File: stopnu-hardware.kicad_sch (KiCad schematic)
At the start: 19 parts, among them CN1 SM04B-SRSS-TB (LF)(SN), CN2 OQ0232510000G, CN3 OQ0232510000G, CN4 OQ0232510000G, CN5 OQ0232510000G, CN6 OQ0232510000G, CN7 OQ0232510000G, CN8 OQ0232510000G, J1 Conn_02x15_Odd_Even

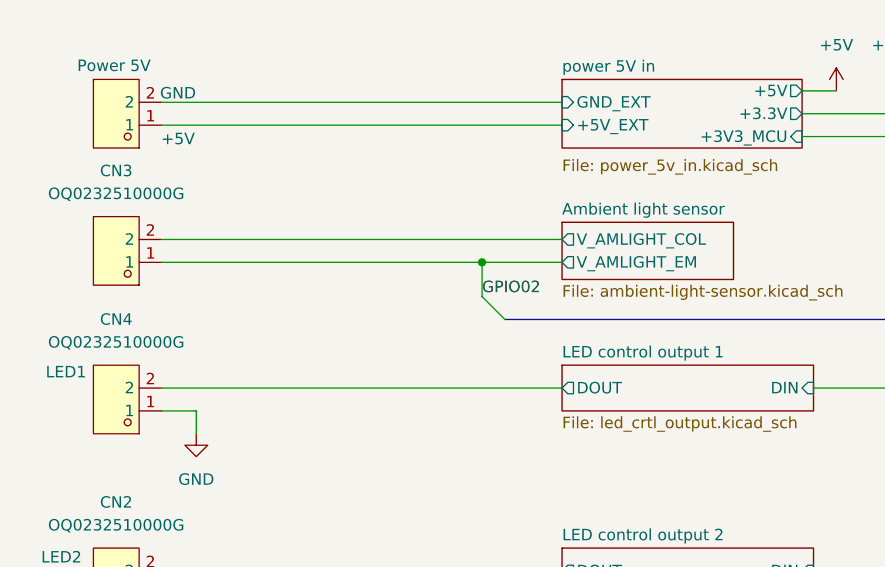
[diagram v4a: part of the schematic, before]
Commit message: Changed ambient light sensor to pull-up design.
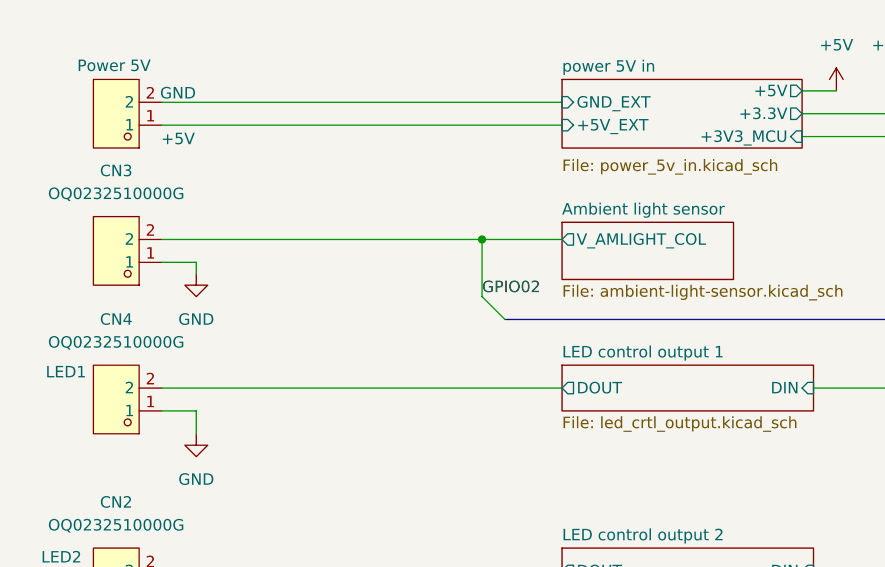
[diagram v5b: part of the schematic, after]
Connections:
- net Ambient light sensor/V_AMLIGHT_COL is gone; now on net GPIO02: CN3.2
- net GND: now also CN3.1
- net GPIO02: no longer CN3.1
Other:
- sheet Ambient light sensor ports: added none; removed V_AMLIGHT_EM
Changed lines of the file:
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@@
 	)
 	(junction
-		(at 68.58 57.15)
+		(at 68.58 54.61)
 		(diameter 0)
 		(color 0 0 0 0)
@@
 	(wire
 		(pts
-			(xy 68.58 57.15) (xy 77.47 57.15)
-		)
-		(stroke
-			(width 0)
-			(type default)
-		)
-	)
-	(wire
-		(pts
 			(xy 219.71 111.76) (xy 219.71 124.46)
 		)
@@
 	(wire
 		(pts
-			(xy 33.02 54.61) (xy 77.47 54.61)
+			(xy 33.02 54.61) (xy 68.58 54.61)
 		)
 		(stroke
@@
 		)
 	)
+	(wire
+		(pts
+			(xy 36.83 57.15) (xy 36.83 58.42)
+		)
+		(stroke
+			(width 0)
+			(type default)
+		)
+	)
 	(bus
 		(pts
@@
 	(wire
 		(pts
-			(xy 40.64 157.48) (xy 40.64 161.29)
+			(xy 68.58 54.61) (xy 77.47 54.61)
 		)
 		(stroke
@@
 	(wire
 		(pts
-			(xy 26.67 123.19) (xy 26.67 127)
+			(xy 40.64 157.48) (xy 40.64 161.29)
 		)
 		(stroke
@@
 	(wire
 		(pts
-			(xy 33.02 39.37) (xy 77.47 39.37)
+			(xy 26.67 123.19) (xy 26.67 127)
 		)
 		(stroke
@@
 		)
 	)
-	(bus
+	(wire
 		(pts
-			(xy 142.24 88.9) (xy 142.24 93.98)
+			(xy 33.02 39.37) (xy 77.47 39.37)
 		)
 		(stroke
@@
 	(bus
 		(pts
-			(xy 142.24 44.45) (xy 142.24 46.99)
+			(xy 142.24 88.9) (xy 142.24 93.98)
 		)
 		(stroke
@@
 		)
 	)
-	(wire
+	(bus
 		(pts
-			(xy 104.14 40.64) (xy 114.3 40.64)
+			(xy 142.24 44.45) (xy 142.24 46.99)
 		)
 		(stroke
@@
 	(wire
 		(pts
-			(xy 33.02 57.15) (xy 68.58 57.15)
+			(xy 104.14 40.64) (xy 114.3 40.64)
 		)
 		(stroke
@@
 	(wire
 		(pts
-			(xy 68.58 57.15) (xy 68.58 60.96)
+			(xy 68.58 54.61) (xy 68.58 60.96)
 		)
 		(stroke
@@
 		)
 	)
+	(wire
+		(pts
+			(xy 33.02 57.15) (xy 36.83 57.15)
+		)
+		(stroke
+			(width 0)
+			(type default)
+		)
+	)
 	(bus
 		(pts
@@
 	)
 	(symbol
+		(lib_id "power:GND")
+		(at 36.83 58.42 0)
+		(unit 1)
+		(exclude_from_sim no)
+		(in_bom yes)
+		(on_board yes)
+		(dnp no)
+		(property "Reference" "#PWR055"
+			(at 36.83 64.77 0)
+			(effects
+				(font
+					(size 1.27 1.27)
+				)
+				(hide yes)
+			)
+		)
+		(property "Value" "GND"
+			(at 36.83 63.5 0)
+			(effects
+				(font
+					(size 1.27 1.27)
+				)
+			)
+		)
+		(property "Footprint" ""
+			(at 36.83 58.42 0)
+			(effects
+				(font
+					(size 1.27 1.27)
+				)
+				(hide yes)
+			)
+		)
+		(property "Datasheet" ""
+			(at 36.83 58.42 0)
+			(effects
+				(font
+					(size 1.27 1.27)
+				)
+				(hide yes)
+			)
+		)
+		(property "Description" "Power symbol creates a global label with name \"GND\" , ground"
+			(at 36.83 58.42 0)
+			(effects
+				(font
+					(size 1.27 1.27)
+				)
+				(hide yes)
+			)
+		)
+		(pin "1"
+		)
+		(instances
+			(project "stopnu-hardware"
+				(path "/4ab90003-ea4c-4878-8117-f834ac24f8d9"
+					(reference "#PWR055")
+					(unit 1)
+				)
+			)
+		)
+	)
+	(symbol
 		(lib_id "Connector_Generic:Conn_02x15_Odd_Even")
 		(at 198.12 119.38 90)
@@
 			(effects
 				(font
-					(size 1.27 1.27)
-				)
-				(justify left)
-			)
-		)
-		(pin "V_AMLIGHT_EM" output
-			(at 77.47 57.15 180)
-			(effects
-				(font

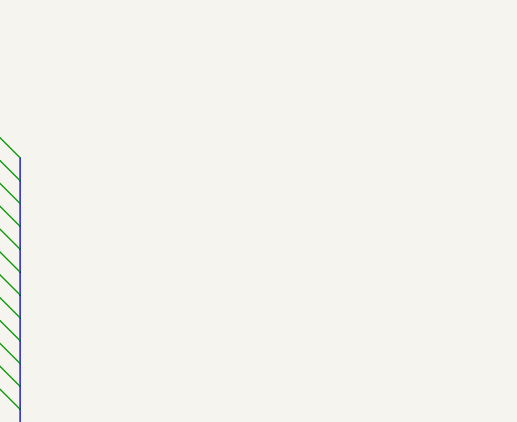
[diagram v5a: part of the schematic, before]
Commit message: Power plane not under top of PCB, add 5V to plug in stuff just in case.
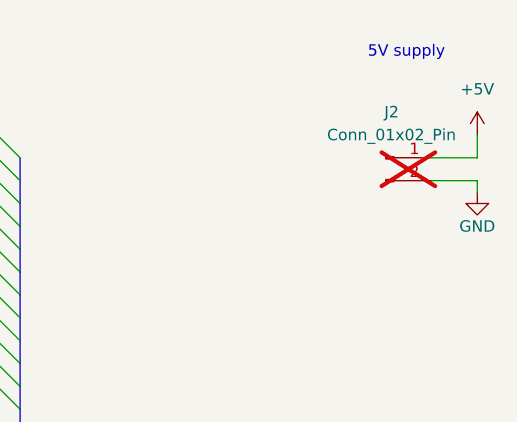
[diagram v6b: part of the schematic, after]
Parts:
- added J2: Conn_01x02_Pin, Connector_PinHeader_2.54mm:PinHeader_1x02_P2.54mm_Vertical, symbol Connector:Conn_01x02_Pin
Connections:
- net +5V: now also J2.1 (Pin_1)
- net GND: now also J2.2 (Pin_2)
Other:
- note added: "5V supply"

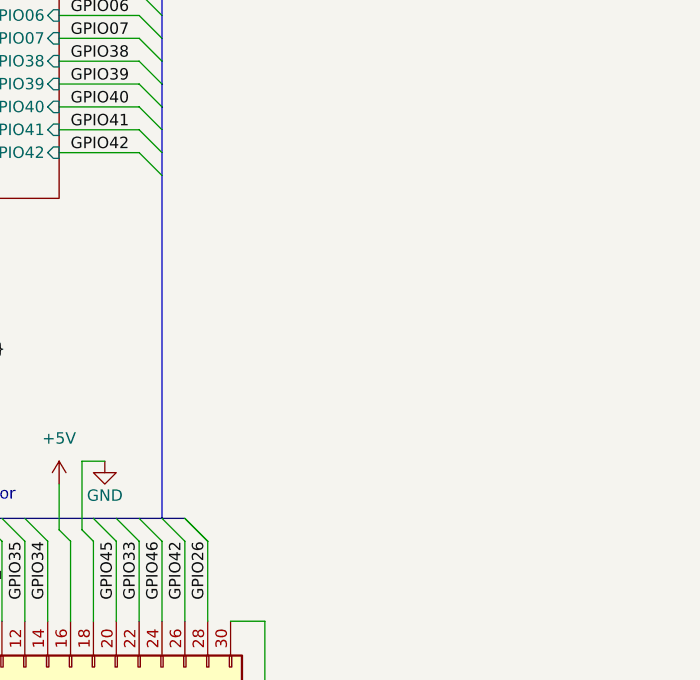
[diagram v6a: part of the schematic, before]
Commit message: Initial MPU6050 addition.
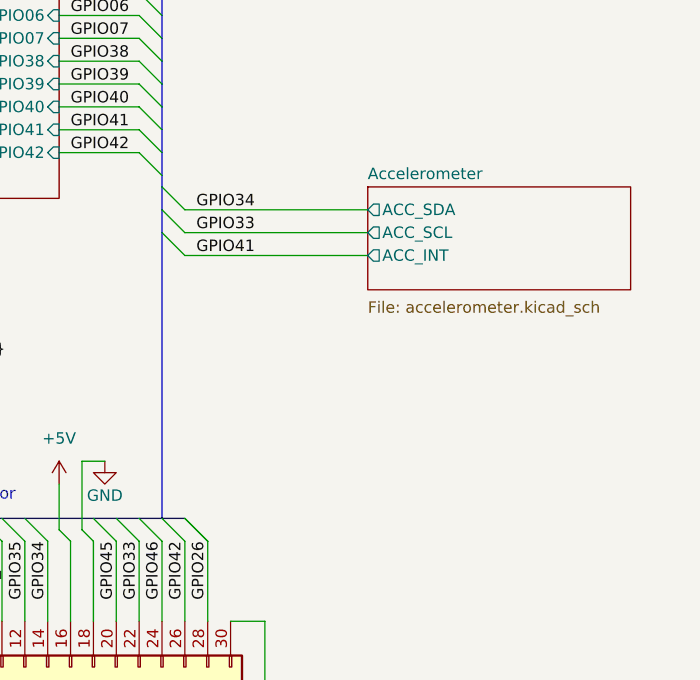
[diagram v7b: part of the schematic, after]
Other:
- added sheet Accelerometer (accelerometer.kicad_sch)
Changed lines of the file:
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@@
 	)
 	(bus_entry
+		(at 208.28 66.04)
+		(size 2.54 2.54)
+		(stroke
+			(width 0)
+			(type default)
+		)
+	)
+	(bus_entry
 		(at 142.24 41.91)
 		(size 2.54 -2.54)
@@
 	)
 	(bus_entry
+		(at 208.28 63.5)
+		(size 2.54 2.54)
+		(stroke
+			(width 0)
+			(type default)
+		)
+	)
+	(bus_entry
 		(at 142.24 49.53)
 		(size 2.54 -2.54)
@@
 	)
 	(bus_entry
+		(at 208.28 68.58)
+		(size 2.54 2.54)
+		(stroke
+			(width 0)
+			(type default)
+		)
+	)
+	(bus_entry
 		(at 142.24 59.69)
 		(size 2.54 -2.54)
@@
 		)
 	)
+	(bus
+		(pts
+			(xy 208.28 66.04) (xy 208.28 68.58)
+		)
+		(stroke
+			(width 0)
+			(type default)
+		)
+	)
 	(wire
 		(pts
@@
 	(bus
 		(pts
-			(xy 208.28 62.23) (xy 208.28 100.33)
+			(xy 208.28 62.23) (xy 208.28 63.5)
 		)
 		(stroke
@@
 	(wire
 		(pts
+			(xy 210.82 66.04) (xy 231.14 66.04)
+		)
+		(stroke
+			(width 0)
+			(type default)
+		)
+	)
+	(wire
+		(pts
 			(xy 259.08 36.83) (xy 259.08 38.1)
 		)
@@
 		)
 	)
+	(bus
+		(pts
+			(xy 208.28 68.58) (xy 208.28 100.33)
+		)
+		(stroke
+			(width 0)
+			(type default)
+		)
+	)
 	(wire
 		(pts
@@
 	(wire
 		(pts
+			(xy 210.82 71.12) (xy 231.14 71.12)
+		)
+		(stroke
+			(width 0)
+			(type default)
+		)
+	)
+	(wire
+		(pts
 			(xy 198.12 102.87) (xy 198.12 111.76)
 		)
@@
 	(bus
 		(pts
+			(xy 208.28 63.5) (xy 208.28 66.04)
+		)
+		(stroke
+			(width 0)
+			(type default)
+		)
+	)
+	(bus
+		(pts
 			(xy 190.5 134.62) (xy 193.04 134.62)
 		)
@@
 	(wire
 		(pts
+			(xy 210.82 68.58) (xy 231.14 68.58)
+		)
+		(stroke
+			(width 0)
+			(type default)
+		)
+	)
+	(wire
+		(pts
 			(xy 36.83 93.98) (xy 36.83 96.52)
 		)
@@
 		)
 	)
+	(label "GPIO41"
+		(at 212.09 71.12 0)
+		(effects
+			(font
+				(size 1.27 1.27)
+			)
+			(justify left bottom)
+		)
+	)
 	(label "GPIO40"
 		(at 185.42 132.08 90)
@@
 		)
 	)
+	(label "GPIO34"
+		(at 212.09 66.04 0)
+		(effects
+			(font
+				(size 1.27 1.27)
+			)
+			(justify left bottom)
+		)
+	)
 	(label "MCU_RST"
 		(at 144.78 54.61 0)
@@
 		)
 	)
+	(label "GPIO33"
+		(at 212.09 68.58 0)
+		(effects
+			(font
+				(size 1.27 1.27)
+			)
+			(justify left bottom)
+		)
+	)
 	(label "GPIO46"
 		(at 208.28 102.87 270)
@@
 				)
 			)
+		)
+	)
+	(sheet
+		(at 231.14 63.5)
+		(size 29.21 11.43)
+		(exclude_from_sim no)
+		(in_bom yes)
+		(on_board yes)
+		(dnp no)
+		(fields_autoplaced yes)
+		(stroke
+			(width 0.1524)
+			(type solid)
+		)
+		(fill
+			(color 0 0 0 0.0000)
+		)
+		(property "Sheetname" "Accelerometer"
+			(at 231.14 62.7884 0)
+			(effects
+				(font
+					(size 1.27 1.27)
+				)
+				(justify left bottom)
+			)
+		)
+		(property "Sheetfile" "accelerometer.kicad_sch"
+			(at 231.14 76.1496 0)
+			(effects
+				(font
+					(size 1.27 1.27)
+				)
+				(justify left top)
+			)
+		)
+		(pin "ACC_INT" output
+			(at 231.14 71.12 180)
+			(effects
+				(font
+					(size 1.27 1.27)
+				)
+				(justify left)
+			)
+		)
+		(pin "ACC_SCL" output
+			(at 231.14 68.58 180)
+			(effects
+				(font
+					(size 1.27 1.27)
+				)
+				(justify left)
+			)
+		)
+		(pin "ACC_SDA" output
+			(at 231.14 66.04 180)
+			(effects
+				(font
+					(size 1.27 1.27)
+				)
+				(justify left)
+			)
+		)
+		(instances
+			(project "stopnu-hardware"
+				(path "/4ab90003-ea4c-4878-8117-f834ac24f8d9"
+					(page "11")
+				)
+			)

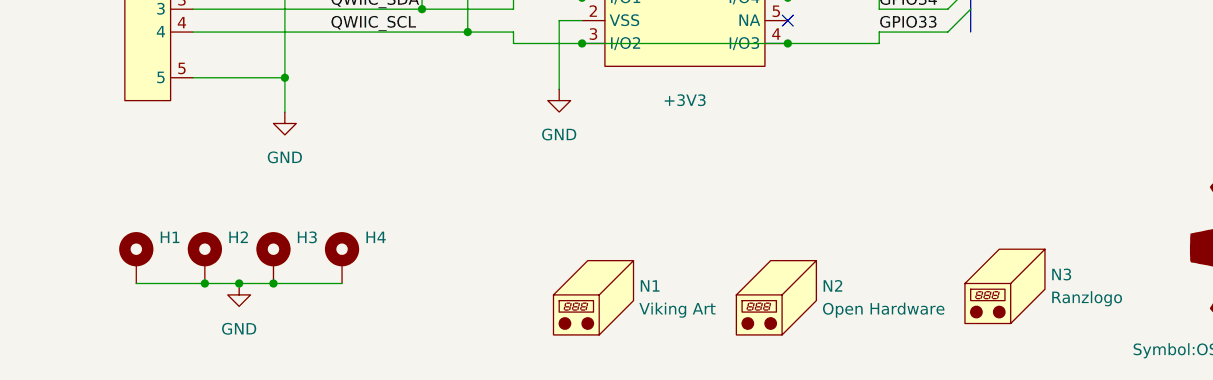
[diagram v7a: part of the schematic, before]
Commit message: Fixed fabrication files, so PCBA will work with the correct rotation of the components.
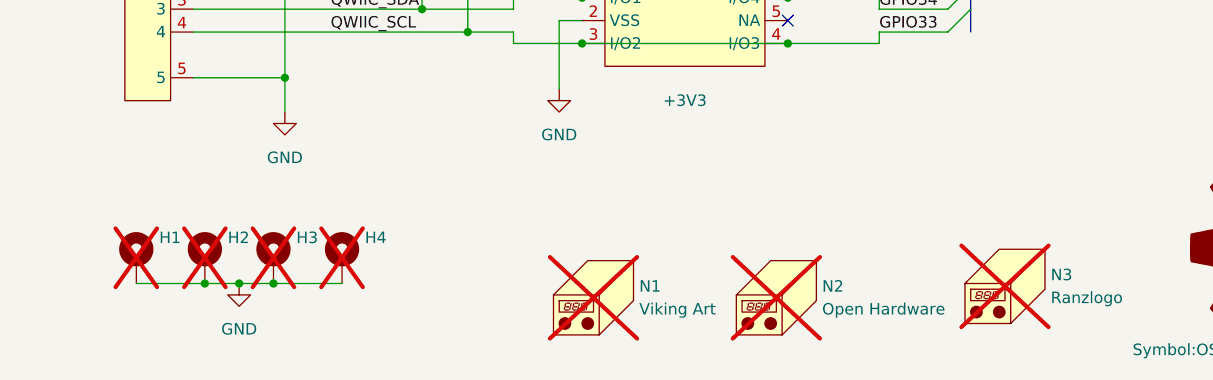
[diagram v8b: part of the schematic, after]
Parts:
- H1, H2, H3, H4: now not fitted
- J1: Rotation Offset (none) -> 90
- N1, N2, N3: now not fitted; now left out of the parts list
